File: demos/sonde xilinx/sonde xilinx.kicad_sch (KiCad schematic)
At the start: 25 parts, among them J1 DB25MALE, J2 DB9MALE, P1 CONN_6, U1 74LS125, U2 74LS125

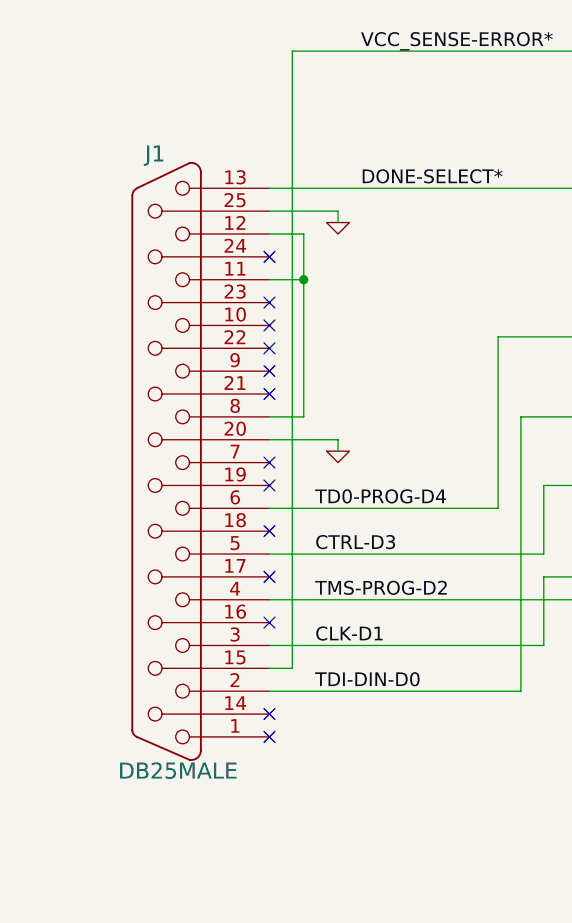
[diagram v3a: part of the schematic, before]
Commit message: Demos: update to last changes in file format.
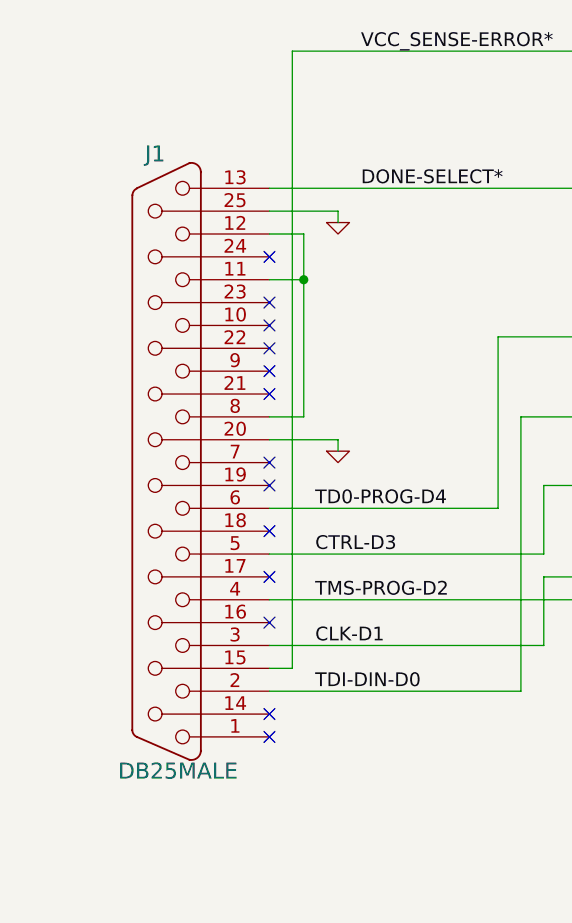
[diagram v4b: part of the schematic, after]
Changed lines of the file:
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@@
-(kicad_sch (version 20210621) (generator eeschema)
+(kicad_sch (version 20211123) (generator eeschema)
   (paper "A4")
   (title_block
@@
     (rev "1")
   )
-  (junction (at 147.32 25.4) (diameter 1.016) (color 0 0 0 0))
-  (junction (at 210.82 72.39) (diameter 1.016) (color 0 0 0 0))
-  (junction (at 205.74 77.47) (diameter 1.016) (color 0 0 0 0))
-  (junction (at 149.86 48.26) (diameter 1.016) (color 0 0 0 0))
-  (junction (at 157.48 25.4) (diameter 1.016) (color 0 0 0 0))
-  (junction (at 59.69 50.8) (diameter 1.016) (color 0 0 0 0))
-  (junction (at 154.94 25.4) (diameter 1.016) (color 0 0 0 0))
-  (junction (at 160.02 48.26) (diameter 1.016) (color 0 0 0 0))
-  (junction (at 259.08 91.44) (diameter 1.016) (color 0 0 0 0))
-  (junction (at 165.1 25.4) (diameter 1.016) (color 0 0 0 0))
-  (junction (at 259.08 101.6) (diameter 1.016) (color 0 0 0 0))
-  (junction (at 29.21 182.88) (diameter 1.016) (color 0 0 0 0))
-  (junction (at 29.21 166.37) (diameter 1.016) (color 0 0 0 0))
-  (junction (at 160.02 83.82) (diameter 1.016) (color 0 0 0 0))
-  (junction (at 149.86 40.64) (diameter 1.016) (color 0 0 0 0))
-  (junction (at 160.02 66.04) (diameter 1.016) (color 0 0 0 0))
-  (junction (at 208.28 74.93) (diameter 1.016) (color 0 0 0 0))
-  (junction (at 259.08 96.52) (diameter 1.016) (color 0 0 0 0))
-  (junction (at 160.02 106.68) (diameter 1.016) (color 0 0 0 0))
-  (junction (at 121.92 73.66) (diameter 1.016) (color 0 0 0 0))
-  (junction (at 213.36 69.85) (diameter 1.016) (color 0 0 0 0))
-  (junction (at 29.21 158.75) (diameter 1.016) (color 0 0 0 0))
-  (junction (at 194.31 25.4) (diameter 1.016) (color 0 0 0 0))
-  (junction (at 29.21 175.26) (diameter 1.016) (color 0 0 0 0))
-  (junction (at 121.92 91.44) (diameter 1.016) (color 0 0 0 0))
-  (junction (at 29.21 149.86) (diameter 1.016) (color 0 0 0 0))
-  (junction (at 149.86 25.4) (diameter 1.016) (color 0 0 0 0))
+  (junction (at 259.08 91.44) (diameter 1.016) (color 0 0 0 0)
+  )
+  (junction (at 194.31 25.4) (diameter 1.016) (color 0 0 0 0)
+  )
+  (junction (at 213.36 69.85) (diameter 1.016) (color 0 0 0 0)
+  )
+  (junction (at 29.21 182.88) (diameter 1.016) (color 0 0 0 0)
+  )
+  (junction (at 160.02 83.82) (diameter 1.016) (color 0 0 0 0)
+  )
+  (junction (at 59.69 50.8) (diameter 1.016) (color 0 0 0 0)
+  )
+  (junction (at 29.21 166.37) (diameter 1.016) (color 0 0 0 0)
+  )
+  (junction (at 149.86 40.64) (diameter 1.016) (color 0 0 0 0)
+  )
+  (junction (at 121.92 91.44) (diameter 1.016) (color 0 0 0 0)
+  )
+  (junction (at 160.02 106.68) (diameter 1.016) (color 0 0 0 0)
+  )
+  (junction (at 149.86 25.4) (diameter 1.016) (color 0 0 0 0)
+  )
+  (junction (at 157.48 25.4) (diameter 1.016) (color 0 0 0 0)
+  )
+  (junction (at 205.74 77.47) (diameter 1.016) (color 0 0 0 0)
+  )
+  (junction (at 208.28 74.93) (diameter 1.016) (color 0 0 0 0)
+  )
+  (junction (at 259.08 101.6) (diameter 1.016) (color 0 0 0 0)
+  )
+  (junction (at 160.02 66.04) (diameter 1.016) (color 0 0 0 0)
+  )
+  (junction (at 29.21 158.75) (diameter 1.016) (color 0 0 0 0)
+  )
+  (junction (at 29.21 149.86) (diameter 1.016) (color 0 0 0 0)
+  )
+  (junction (at 259.08 96.52) (diameter 1.016) (color 0 0 0 0)
+  )
+  (junction (at 154.94 25.4) (diameter 1.016) (color 0 0 0 0)
+  )
+  (junction (at 29.21 175.26) (diameter 1.016) (color 0 0 0 0)
+  )
+  (junction (at 210.82 72.39) (diameter 1.016) (color 0 0 0 0)
+  )
+  (junction (at 121.92 73.66) (diameter 1.016) (color 0 0 0 0)
+  )
+  (junction (at 149.86 48.26) (diameter 1.016) (color 0 0 0 0)
+  )
+  (junction (at 160.02 48.26) (diameter 1.016) (color 0 0 0 0)
+  )
+  (junction (at 147.32 25.4) (diameter 1.016) (color 0 0 0 0)
+  )
+  (junction (at 165.1 25.4) (diameter 1.016) (color 0 0 0 0)
+  )
   (no_connect (at 54.61 175.26))
   (no_connect (at 55.88 88.9))

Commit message: Demo update
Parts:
- U: renamed from J1; value DB25MALE -> (none); footprint Connector_Dsub:DSUB-25_Male_EdgeMount_P2.77mm -> (none)
- U: renamed from R1; value 100 -> (none); footprint Resistor_THT:R_Axial_DIN0207_L6.3mm_D2.5mm_P10.16mm_Horizontal -> (none)
- U: renamed from R4; value 47 -> (none); footprint Resistor_THT:R_Axial_DIN0207_L6.3mm_D2.5mm_P10.16mm_Horizontal -> (none)
- U: renamed from R6; value 100 -> (none); footprint Resistor_THT:R_Axial_DIN0207_L6.3mm_D2.5mm_P10.16mm_Horizontal -> (none)
- U: renamed from R10; value 100 -> (none); footprint Resistor_THT:R_Axial_DIN0207_L6.3mm_D2.5mm_P10.16mm_Horizontal -> (none)
- U: renamed from R9; value 100 -> (none); footprint Resistor_THT:R_Axial_DIN0207_L6.3mm_D2.5mm_P10.16mm_Horizontal -> (none)
- U: renamed from U2; value 74LS125 -> (none); footprint Package_DIP:DIP-14_W7.62mm_LongPads -> (none)
- U: renamed from U1; value 74LS125 -> (none); footprint Package_DIP:DIP-14_W7.62mm_LongPads -> (none)
- U: renamed from D1; value BAT46 -> (none); footprint Diode_THT:D_A-405_P7.62mm_Horizontal -> (none)
- U: renamed from D2; value BAT46 -> (none); footprint Diode_THT:D_A-405_P7.62mm_Horizontal -> (none)
- U: renamed from R2; value 5,1K -> (none); footprint Resistor_THT:R_Axial_DIN0207_L6.3mm_D2.5mm_P10.16mm_Horizontal -> (none)
- U: renamed from R5; value 1K -> (none); footprint Resistor_THT:R_Axial_DIN0207_L6.3mm_D2.5mm_P10.16mm_Horizontal -> (none)
- U: renamed from R14; value 100 -> (none); footprint Resistor_THT:R_Axial_DIN0207_L6.3mm_D2.5mm_P10.16mm_Horizontal -> (none)
- U: renamed from C4; value 100pF -> (none); footprint Capacitor_THT:C_Disc_D5.1mm_W3.2mm_P5.00mm -> (none)
- U: renamed from C1; value 1uF -> (none); footprint Capacitor_THT:C_Axial_L5.1mm_D3.1mm_P12.50mm_Horizontal -> (none)
- U: renamed from P1; value CONN_6 -> (none); footprint Connector_PinHeader_2.54mm:PinHeader_1x06_P2.54mm_Vertical -> (none)
- U: renamed from J2; value DB9MALE -> (none); footprint Connector_Dsub:DSUB-9_Male_EdgeMount_P2.77mm -> (none)
- U: renamed from R11; value 100 -> (none); footprint Resistor_THT:R_Axial_DIN0207_L6.3mm_D2.5mm_P10.16mm_Horizontal -> (none)
- U: renamed from R7; value 100 -> (none); footprint Resistor_THT:R_Axial_DIN0207_L6.3mm_D2.5mm_P10.16mm_Horizontal -> (none)
- U: renamed from R8; value 100 -> (none); footprint Resistor_THT:R_Axial_DIN0207_L6.3mm_D2.5mm_P10.16mm_Horizontal -> (none)
- U: renamed from R13; value 100 -> (none); footprint Resistor_THT:R_Axial_DIN0207_L6.3mm_D2.5mm_P10.16mm_Horizontal -> (none)
- U: renamed from R12; value 100 -> (none); footprint Resistor_THT:R_Axial_DIN0207_L6.3mm_D2.5mm_P10.16mm_Horizontal -> (none)
- U: renamed from C3; value 100pF -> (none); footprint Capacitor_THT:C_Disc_D5.1mm_W3.2mm_P5.00mm -> (none)
- U: renamed from C2; value 100pF -> (none); footprint Capacitor_THT:C_Disc_D5.1mm_W3.2mm_P5.00mm -> (none)
- U: renamed from C5; value 100pF -> (none); footprint Capacitor_THT:C_Disc_D5.1mm_W3.2mm_P5.00mm -> (none)
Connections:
- net GND: now also U.1 (E), U.1 (E), U.1 (E), U.2 (D), U.2 (D), U.2 (D); no longer U.10 (E), U.12 (D), U.13 (E), U.4 (E), U.5 (D), U.9 (D)
- net at U.1: now also U.2 (D); no longer U.9 (D)
- net at U.1: now also U.2 (D); no longer U.12 (D)
- net at U.1: now also U.2 (D); no longer U.5 (D)
- net at U.1, U.2: now also U.3 (O); no longer U.6 (O)
- net at U.1, U.2: now also U.3 (O); no longer U.8 (O)
- net at U.1, U.2: now also U.3 (O); no longer U.11 (O)
- new net: U.1, U.1 (E), U.1 (E), U.1 (E)

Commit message: Demos update
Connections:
- net GND: now also U.10 (E), U.12 (D), U.13 (E), U.4 (E), U.5 (D), U.9 (D); no longer U.1 (E), U.1 (E), U.1 (E), U.2 (D), U.2 (D), U.2 (D)
- net at U.1: now also U.9 (D); no longer U.2 (D)
- net at U.1: now also U.12 (D); no longer U.2 (D)
- net at U.1: now also U.5 (D); no longer U.2 (D)
- net at U.1, U.2: now also U.6 (O); no longer U.3 (O)
- net at U.1, U.2: now also U.8 (O); no longer U.3 (O)
- net at U.1, U.2: now also U.11 (O); no longer U.3 (O)
- new net: U.1, U.10 (E), U.13 (E), U.4 (E)
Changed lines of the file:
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@@
-(kicad_sch (version 20220622) (generator eeschema)
+(kicad_sch (version 20220822) (generator eeschema)
   (paper "A4")
   (title_block
@@
     (pin "2")
   )
-  (symbol (lib_id "sonde_xilinx_schlib:74LS125") (at 118.11 40.64 0) (mirror y) (unit 1)
+  (symbol (lib_name "74LS125_2") (lib_id "sonde_xilinx_schlib:74LS125") (at 118.11 40.64 0) (mirror y) (unit 1)
     (in_bom yes) (on_board yes)
     (default_instance (reference "U") (unit 1) (value "") (footprint ""))
@@
     (pin "3")
   )
-  (symbol (lib_id "sonde_xilinx_schlib:74LS125") (at 137.16 48.26 0) (unit 1)
+  (symbol (lib_name "74LS125_1") (lib_id "sonde_xilinx_schlib:74LS125") (at 137.16 48.26 0) (unit 1)
     (in_bom yes) (on_board yes)
     (default_instance (reference "U") (unit 1) (value "") (footprint ""))
@@
     (pin "3")
   )
-  (symbol (lib_id "sonde_xilinx_schlib:74LS125") (at 138.43 66.04 0) (unit 1)
+  (symbol (lib_name "74LS125_6") (lib_id "sonde_xilinx_schlib:74LS125") (at 138.43 66.04 0) (unit 2)
     (in_bom yes) (on_board yes)
     (default_instance (reference "U") (unit 1) (value "") (footprint ""))
@@
     (pin "6")
   )
-  (symbol (lib_id "sonde_xilinx_schlib:74LS125") (at 138.43 83.82 0) (unit 1)
+  (symbol (lib_name "74LS125_7") (lib_id "sonde_xilinx_schlib:74LS125") (at 138.43 83.82 0) (unit 3)
     (in_bom yes) (on_board yes)
     (default_instance (reference "U") (unit 1) (value "") (footprint ""))
@@
     (pin "9")
   )
-  (symbol (lib_id "sonde_xilinx_schlib:74LS125") (at 138.43 106.68 0) (unit 1)
+  (symbol (lib_id "sonde_xilinx_schlib:74LS125") (at 138.43 106.68 0) (unit 4)
     (in_bom yes) (on_board yes)
     (default_instance (reference "U") (unit 1) (value "") (footprint ""))
@@
     (pin "12")
   )
-  (symbol (lib_id "sonde_xilinx_schlib:74LS125") (at 43.18 175.26 0) (unit 1)
+  (symbol (lib_name "74LS125_3") (lib_id "sonde_xilinx_schlib:74LS125") (at 43.18 175.26 0) (unit 2)
     (in_bom yes) (on_board yes)
     (default_instance (reference "U") (unit 1) (value "") (footprint ""))
@@
     (pin "6")
   )
-  (symbol (lib_id "sonde_xilinx_schlib:74LS125") (at 43.18 158.75 0) (unit 1)
+  (symbol (lib_name "74LS125_4") (lib_id "sonde_xilinx_schlib:74LS125") (at 43.18 158.75 0) (unit 3)
     (in_bom yes) (on_board yes)
     (default_instance (reference "U") (unit 1) (value "") (footprint ""))
@@
     (pin "9")
   )
-  (symbol (lib_id "sonde_xilinx_schlib:74LS125") (at 43.18 142.24 0) (unit 1)
-    (in_bom yes) (on_board yes)
-    (default_instance (reference "U") (unit 1) (value "") (footprint ""))
+  (symbol (lib_name "74LS125_5") (lib_id "sonde_xilinx_schlib:74LS125") (at 43.18 142.24 0) (unit 4)
+    (in_bom yes) (on_board yes)
+    (default_instance (reference "U") (unit 1) (value "") (footprint ""))

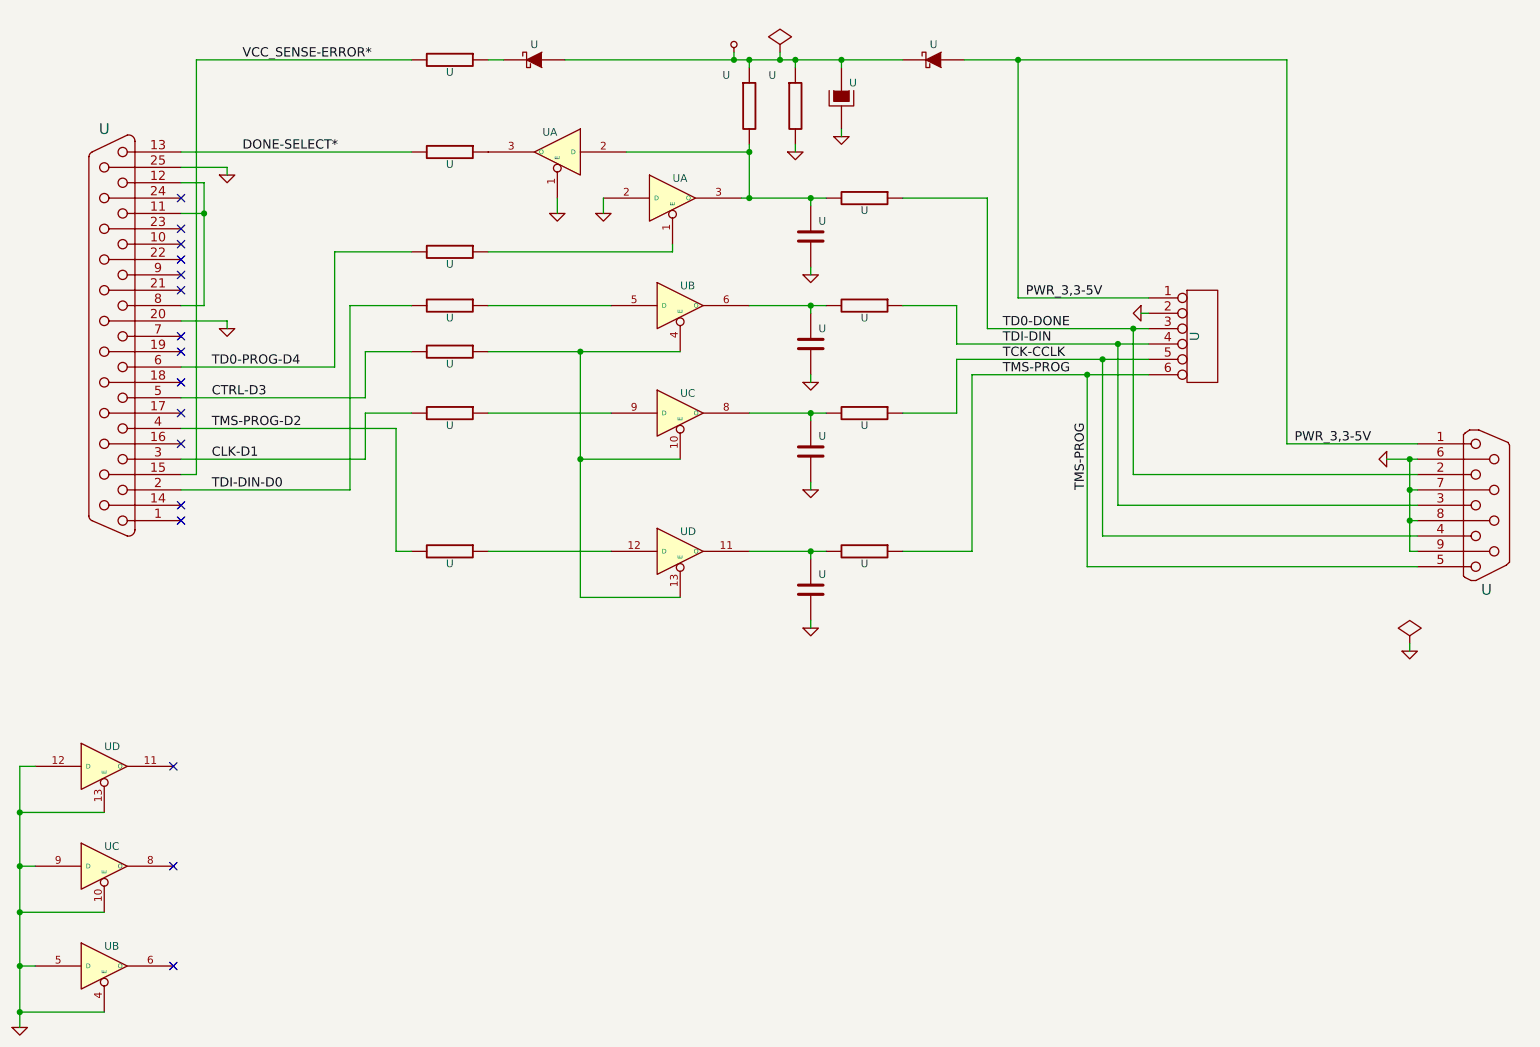
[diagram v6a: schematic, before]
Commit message: Update demos using latest file formats.
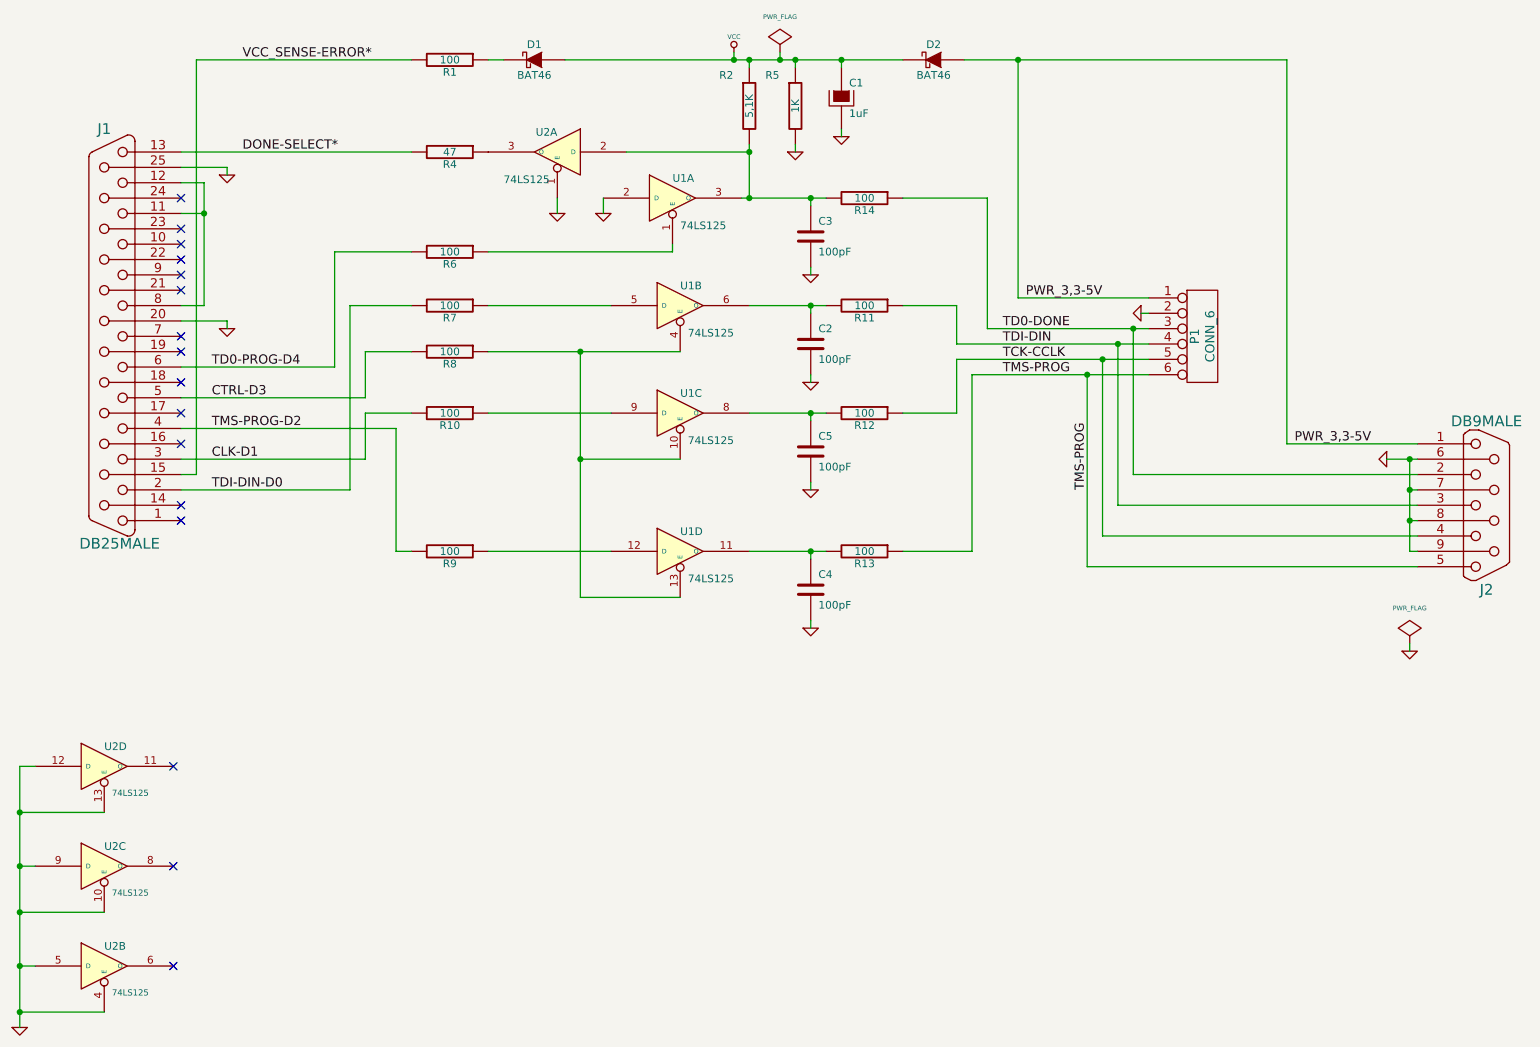
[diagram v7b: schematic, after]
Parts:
- C1: renamed from U; value (none) -> 1uF; footprint (none) -> Capacitor_THT:C_Axial_L5.1mm_D3.1mm_P12.50mm_Horizontal
- C2, C3, C4, C5: renamed from U; value (none) -> 100pF; footprint (none) -> Capacitor_THT:C_Disc_D5.1mm_W3.2mm_P5.00mm
- D1, D2: renamed from U; value (none) -> BAT46; footprint (none) -> Diode_THT:D_A-405_P7.62mm_Horizontal
- J1: renamed from U; value (none) -> DB25MALE; footprint (none) -> Connector_Dsub:DSUB-25_Male_EdgeMount_P2.77mm
- J2: renamed from U; value (none) -> DB9MALE; footprint (none) -> Connector_Dsub:DSUB-9_Male_EdgeMount_P2.77mm
- P1: renamed from U; value (none) -> CONN_6; footprint (none) -> Connector_PinHeader_2.54mm:PinHeader_1x06_P2.54mm_Vertical
- R1, R10, R11, R12, R13, R14, R6, R7, R8, R9: renamed from U; value (none) -> 100; footprint (none) -> Resistor_THT:R_Axial_DIN0207_L6.3mm_D2.5mm_P10.16mm_Horizontal
- R2: renamed from U; value (none) -> 5,1K; footprint (none) -> Resistor_THT:R_Axial_DIN0207_L6.3mm_D2.5mm_P10.16mm_Horizontal
- R4: renamed from U; value (none) -> 47; footprint (none) -> Resistor_THT:R_Axial_DIN0207_L6.3mm_D2.5mm_P10.16mm_Horizontal
- R5: renamed from U; value (none) -> 1K; footprint (none) -> Resistor_THT:R_Axial_DIN0207_L6.3mm_D2.5mm_P10.16mm_Horizontal
- U1, U2: renamed from U; value (none) -> 74LS125; footprint (none) -> Package_DIP:DIP-14_W7.62mm_LongPads
